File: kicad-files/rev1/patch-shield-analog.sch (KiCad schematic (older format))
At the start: 38 parts, among them P1 CONN_1, P10 CONN_1, P11 CONN_1, P12 CONN_1, P13 CONN_1, P14 CONN_1, P15 CONN_1, P16 CONN_1, P17 CONN_1, P18 CONN_20X2, P19 CONN_1, P2 CONN_1, P20 CONN_1, P21 CONN_1, P22 CONN_1, P23 CONN_1, P24 CONN_1, P25 CONN_1, P26 CONN_1, P27 CONN_1, P28 CONN_1, P29 CONN_1, P3 CONN_1, P30 CONN_1, P31 CONN_1, P32 CONN_1, P33 CONN_1, P34 CONN_1, P35 CONN_5X2, P36 ARDUINO_SHIELD, P4 CONN_1, P5 CONN_1, P6 CONN_1, P7 CONN_1, P8 CONN_1, P9 CONN_1

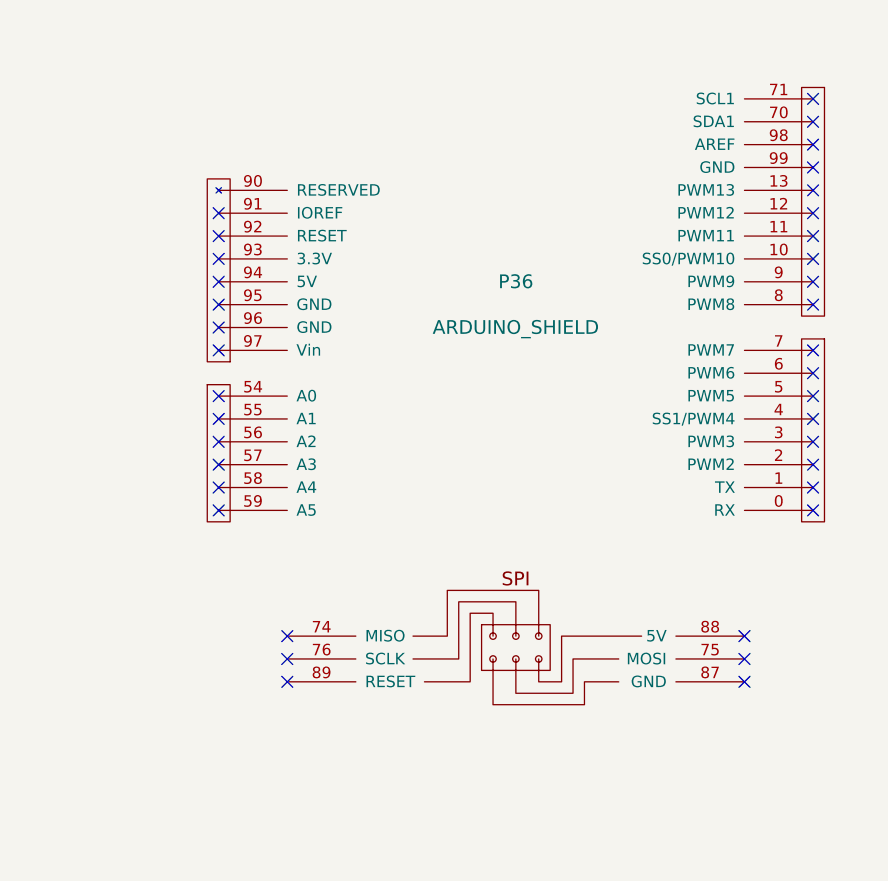
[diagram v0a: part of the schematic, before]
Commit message: route analog patch-shield
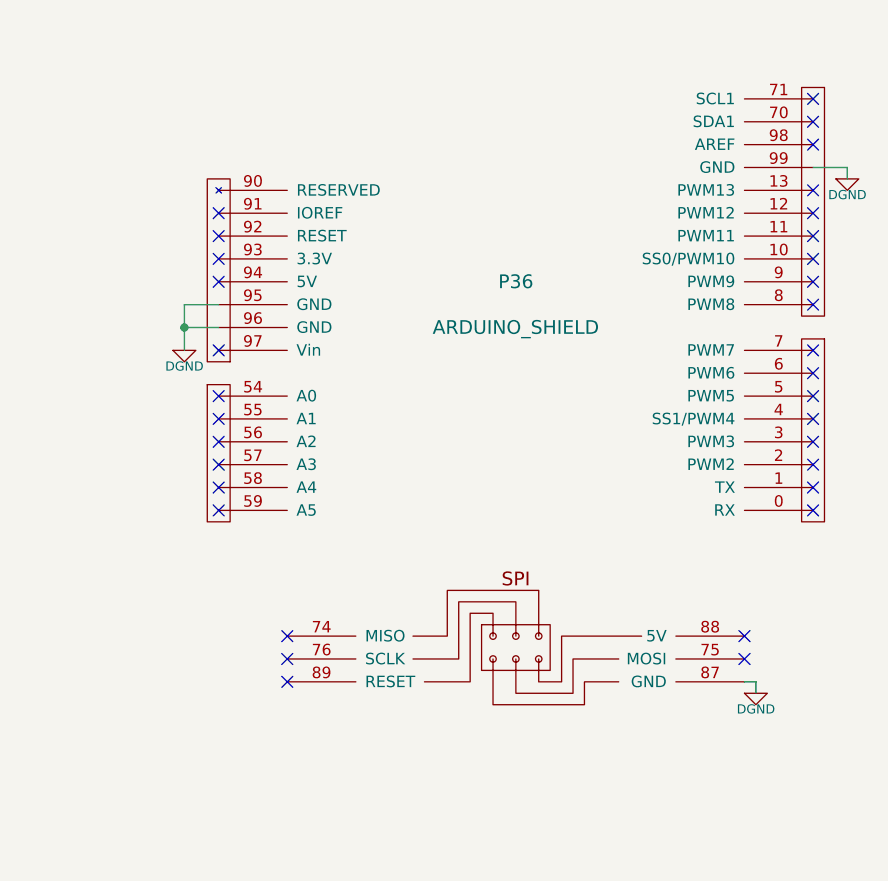
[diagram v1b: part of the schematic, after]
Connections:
- net labels added: DGND
- wire segments 86 -> 93
- no-connect marks 47 -> 43
